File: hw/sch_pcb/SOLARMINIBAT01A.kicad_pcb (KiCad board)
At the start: 2 copper layers, 80.8 x 70.6 mm, 79 parts, among them J1 HEADER_2x03_PARALLEL, J2 WAGO 256 RED, J3 WAGO 256 BLUE, J4 HEADER_2x01_PARALLEL, J5 HEADER_2x03_PARALLEL, J6 HEADER_2x03_PARALLEL, M1 HOLE, M2 HOLE, M3 HOLE, M4 HOLE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

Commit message: Edit PCB
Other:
- rule pad_to_mask_clearance: 0 -> 0.2
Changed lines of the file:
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@@
       (dielectric_constraints no)
     )
-    (pad_to_mask_clearance 0)
+    (pad_to_mask_clearance 0.2)
     (aux_axis_origin 79.756 147.066)
     (pcbplotparams
@@
       (options (clearance outline) (anchor rect))
       (primitives
-    (gr_arc (start 0.402401 0.542868) (mid 0.307344 -0.001001) (end 0.403085 -0.544749) (width 0.4))
+    (gr_arc (start 0.402401 0.542868) (mid 0.307344 -0.001) (end 0.403084 -0.544748) (width 0.4))
         (gr_poly (pts
             (xy 0.405 0.75)
@@
       (options (clearance outline) (anchor rect))
       (primitives
-    (gr_arc (start 0.402401 0.542868) (mid 0.307344 -0.001001) (end 0.403085 -0.544749) (width 0.4))
+    (gr_arc (start 0.402401 0.542868) (mid 0.307344 -0.001) (end 0.403084 -0.544748) (width 0.4))
         (gr_poly (pts
             (xy 0.405 0.75)
@@
       (options (clearance outline) (anchor rect))
       (primitives
-    (gr_arc (start 0.402401 0.542868) (mid 0.307344 -0.001001) (end 0.403085 -0.544749) (width 0.4))
+    (gr_arc (start 0.402401 0.542868) (mid 0.307344 -0.001) (end 0.403084 -0.544748) (width 0.4))
         (gr_poly (pts
             (xy 0.405 0.75)
@@
       (options (clearance outline) (anchor rect))
       (primitives
-    (gr_arc (start 0.402401 0.542868) (mid 0.307344 -0.001001) (end 0.403085 -0.544749) (width 0.4))
+    (gr_arc (start 0.402401 0.542868) (mid 0.307344 -0.001) (end 0.403084 -0.544748) (width 0.4))
         (gr_poly (pts
             (xy 0.405 0.75)
@@
       (options (clearance outline) (anchor rect))
       (primitives
-    (gr_arc (start 0.402401 0.542868) (mid 0.307344 -0.001001) (end 0.403085 -0.544749) (width 0.4))
+    (gr_arc (start 0.402401 0.542868) (mid 0.307344 -0.001) (end 0.403084 -0.544748) (width 0.4))
         (gr_poly (pts
             (xy 0.405 0.75)
@@
       (options (clearance outline) (anchor rect))
       (primitives
-    (gr_arc (start 0.402401 0.542868) (mid 0.307344 -0.001001) (end 0.403085 -0.544749) (width 0.4))
+    (gr_arc (start 0.402401 0.542868) (mid 0.307344 -0.001) (end 0.403084 -0.544748) (width 0.4))
         (gr_poly (pts
             (xy 0.405 0.75)
@@
       (options (clearance outline) (anchor rect))
       (primitives
-    (gr_arc (start 0.402401 0.542868) (mid 0.307344 -0.001001) (end 0.403085 -0.544749) (width 0.4))
+    (gr_arc (start 0.402401 0.542868) (mid 0.307344 -0.001) (end 0.403084 -0.544748) (width 0.4))
         (gr_poly (pts
             (xy 0.405 0.75)
@@
       (options (clearance outline) (anchor rect))
       (primitives
-    (gr_arc (start 0.402401 0.542868) (mid 0.307344 -0.001001) (end 0.403085 -0.544749) (width 0.4))
+    (gr_arc (start 0.402401 0.542868) (mid 0.307344 -0.001) (end 0.403084 -0.544748) (width 0.4))
         (gr_poly (pts
             (xy 0.405 0.75)
@@
       (options (clearance outline) (anchor rect))
       (primitives
-    (gr_arc (start 0.402401 0.542868) (mid 0.307344 -0.001001) (end 0.403085 -0.544749) (width 0.4))
+    (gr_arc (start 0.402401 0.542868) (mid 0.307344 -0.001) (end 0.403084 -0.544748) (width 0.4))
         (gr_poly (pts
             (xy 0.405 0.75)
@@
       (options (clearance outline) (anchor rect))
       (primitives
-    (gr_arc (start 0.402401 0.542868) (mid 0.307344 -0.001001) (end 0.403085 -0.544749) (width 0.4))
+    (gr_arc (start 0.402401 0.542868) (mid 0.307344 -0.001) (end 0.403084 -0.544748) (width 0.4))
         (gr_poly (pts
             (xy 0.405 0.75)
@@
       (options (clearance outline) (anchor rect))
       (primitives
-    (gr_arc (start 0.402401 0.542868) (mid 0.307344 -0.001001) (end 0.403085 -0.544749) (width 0.4))
+    (gr_arc (start 0.402401 0.542868) (mid 0.307344 -0.001) (end 0.403084 -0.544748) (width 0.4))
         (gr_poly (pts
             (xy 0.405 0.75)
@@
       (options (clearance outline) (anchor rect))
       (primitives
-    (gr_arc (start 0.402401 0.542868) (mid 0.307344 -0.001001) (end 0.403085 -0.544749) (width 0.4))
+    (gr_arc (start 0.402401 0.542868) (mid 0.307344 -0.001) (end 0.403084 -0.544748) (width 0.4))
         (gr_poly (pts
             (xy 0.405 0.75)
@@
       (options (clearance outline) (anchor rect))
       (primitives
-    (gr_arc (start 0.402401 0.542868) (mid 0.307344 -0.001001) (end 0.403085 -0.544749) (width 0.4))
+    (gr_arc (start 0.402401 0.542868) (mid 0.307344 -0.001) (end 0.403084 -0.544748) (width 0.4))
         (gr_poly (pts
             (xy 0.405 0.75)
@@
       (options (clearance outline) (anchor rect))
       (primitives
-    (gr_arc (start 0.402401 0.542868) (mid 0.307344 -0.001001) (end 0.403085 -0.544749) (width 0.4))
+    (gr_arc (start 0.402401 0.542868) (mid 0.307344 -0.001) (end 0.403084 -0.544748) (width 0.4))
         (gr_poly (pts
             (xy 0.405 0.75)
@@
       (options (clearance outline) (anchor rect))
       (primitives
-    (gr_arc (start 0.402401 0.542868) (mid 0.307344 -0.001001) (end 0.403085 -0.544749) (width 0.4))
+    (gr_arc (start 0.402401 0.542868) (mid 0.307344 -0.001) (end 0.403084 -0.544748) (width 0.4))
         (gr_poly (pts
             (xy 0.405 0.75)
@@
       (options (clearance outline) (anchor rect))
       (primitives
-    (gr_arc (start 0.402401 0.542868) (mid 0.307344 -0.001001) (end 0.403085 -0.544749) (width 0.4))
+    (gr_arc (start 0.402401 0.542868) (mid 0.307344 -0.001) (end 0.403084 -0.544748) (width 0.4))
         (gr_poly (pts
             (xy 0.405 0.75)

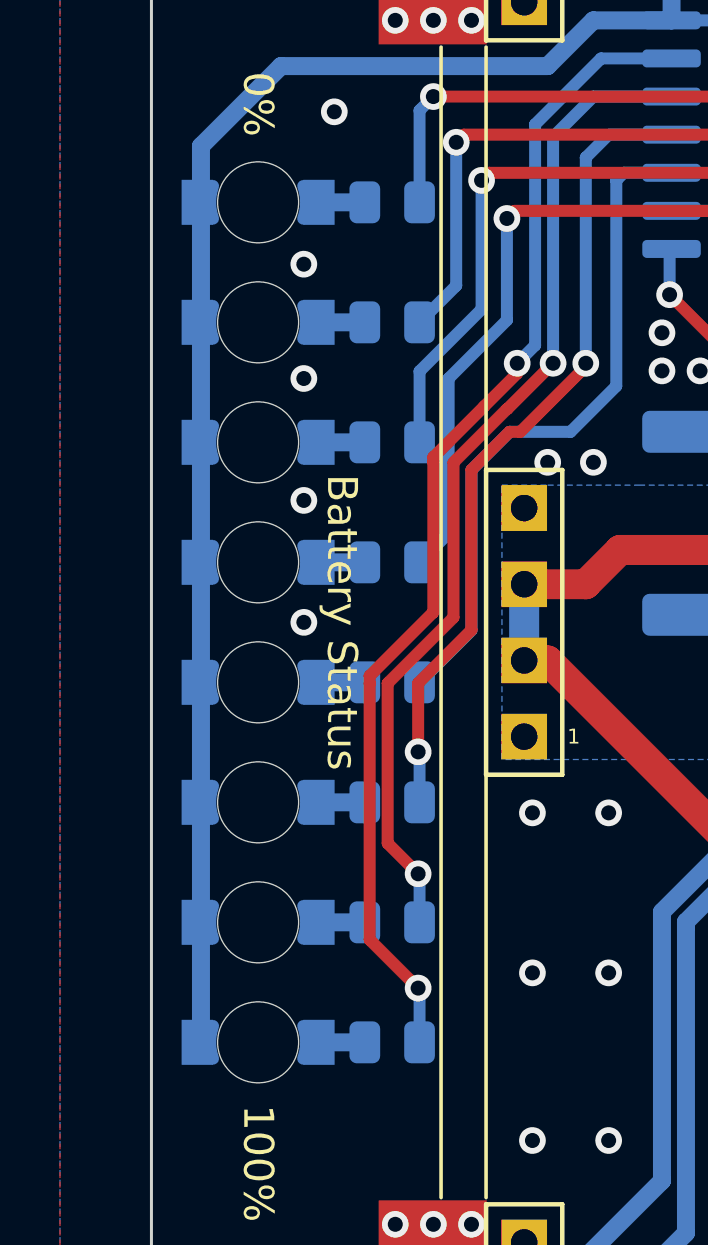
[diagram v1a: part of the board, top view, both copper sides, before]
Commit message: Editing FAB layer
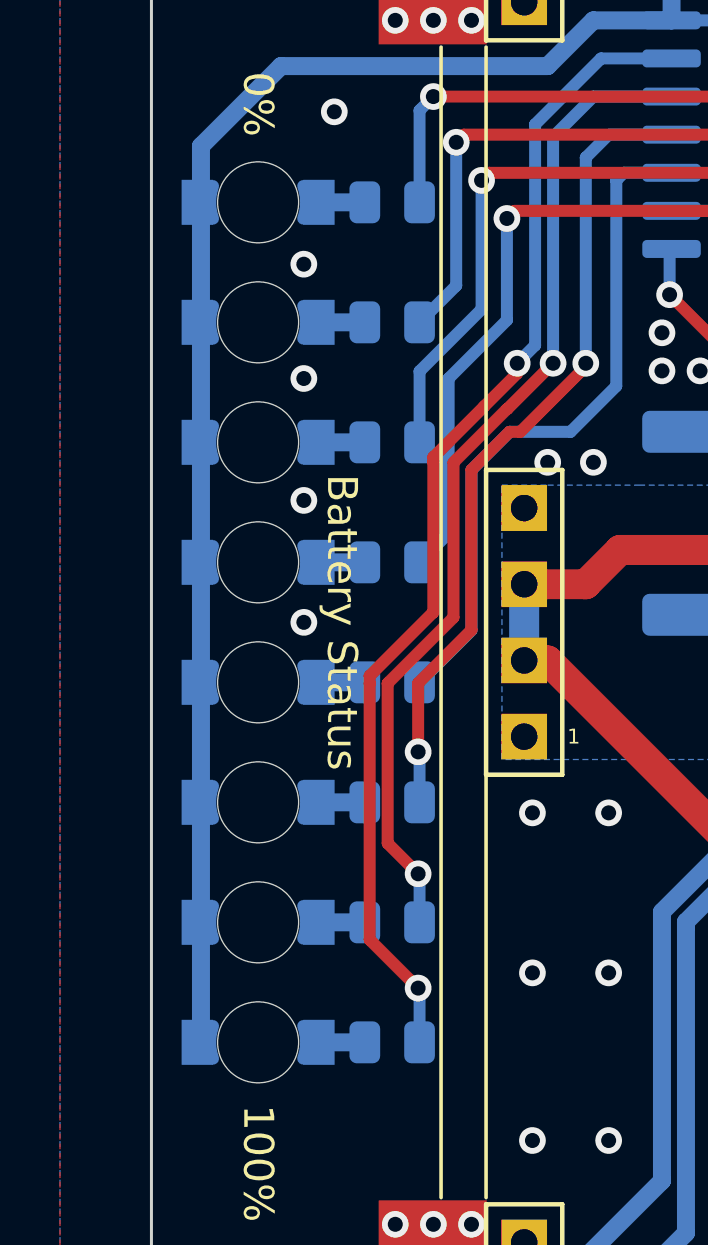
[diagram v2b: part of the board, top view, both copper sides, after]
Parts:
- C13, C17: value 10uF -> 10uF/6V3
- J2: value WAGO 256 RED -> WAGO 256 ORANGE
- R21: value 0R47 -> 0R
- R22: value 560k -> 110k
- R23: value 270k -> 100k
- R5: value 1K -> 1k
